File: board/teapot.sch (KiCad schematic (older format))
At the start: 36 parts, among them P1 BATT, P2 SMA, Q1 TEPT4400, U1 TLV61225, U2 microusb-b, U3 RFM69W, U4 STM32L052K8, U5 HTU21D, U6 MS5637, U7 SWD, Y1 32.768k

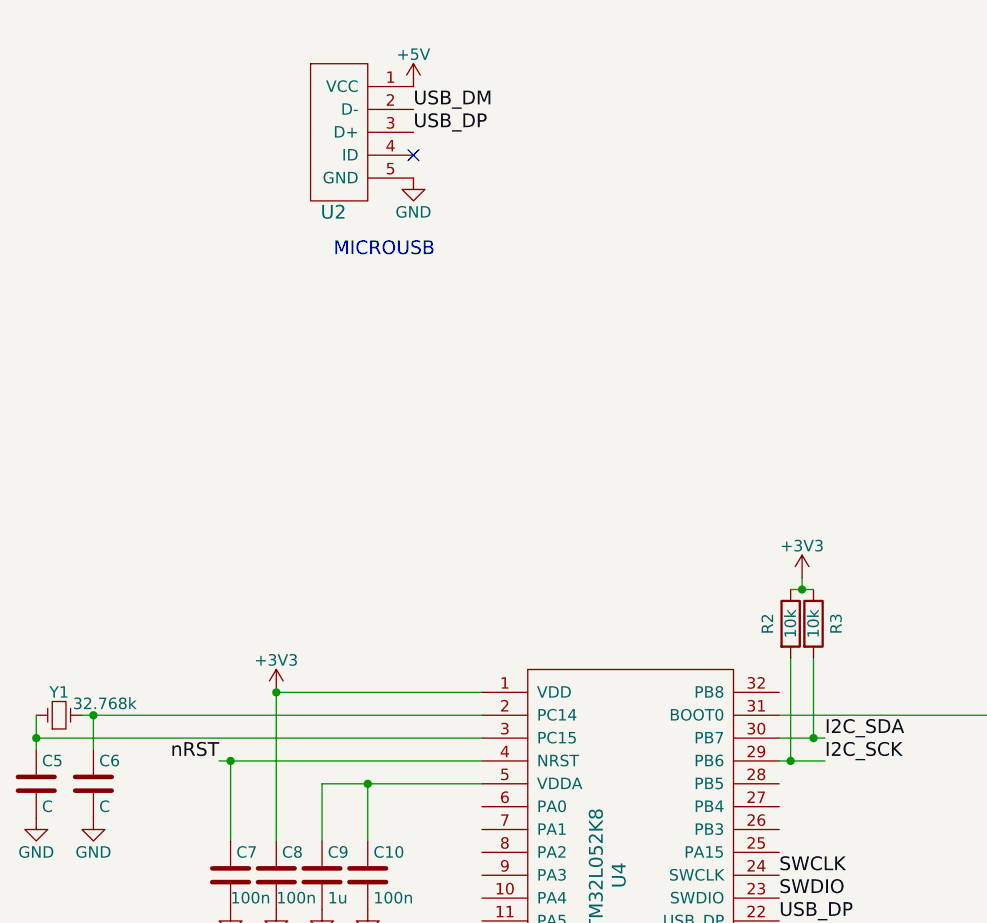
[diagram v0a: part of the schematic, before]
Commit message: Added USB LDO.  Resolves #9
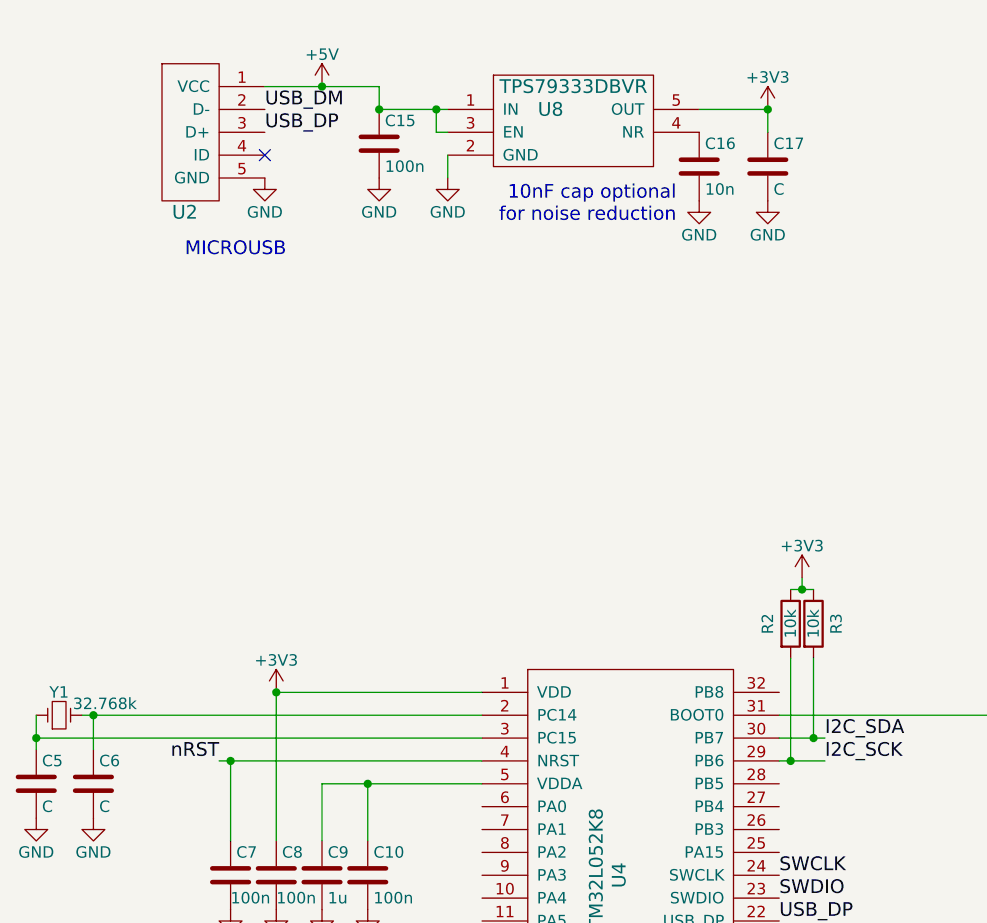
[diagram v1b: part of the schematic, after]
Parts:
- added C15: 100n, symbol C
- added C16: 10n, symbol C
- added C17: C, symbol C
- added U8: TPS79333DBVR, TO_SOT_Packages_SMD:SOT-23-5, symbol TPS79333DBVR
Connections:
- net +3V3: now also C17.1, U8.5 (OUT)
- net +5V: now also C15.1, U8.1 (IN), U8.3 (EN)
- net GND: now also C15.2, C16.2, C17.2, U8.2 (GND)
- new net: C16.1, U8.4 (NR)
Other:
- note added: "10nF cap optional\nfor noise reduction"
- moved on the sheet: U2

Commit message: Added microusb footprint, resolves #6
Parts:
- U2: footprint (none) -> footprints:USB3065
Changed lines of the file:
@@
 F 0 "U2" H 4550 950 60  0000 C CNN
 F 1 "microusb-b" H 4550 850 60  0001 C CNN
-F 2 "" H 4700 1300 60  0000 C CNN
+F 2 "footprints:USB3065" H 4700 1300 60  0001 C CNN
 F 3 "" H 4700 1300 60  0000 C CNN
 	1    4600 1300

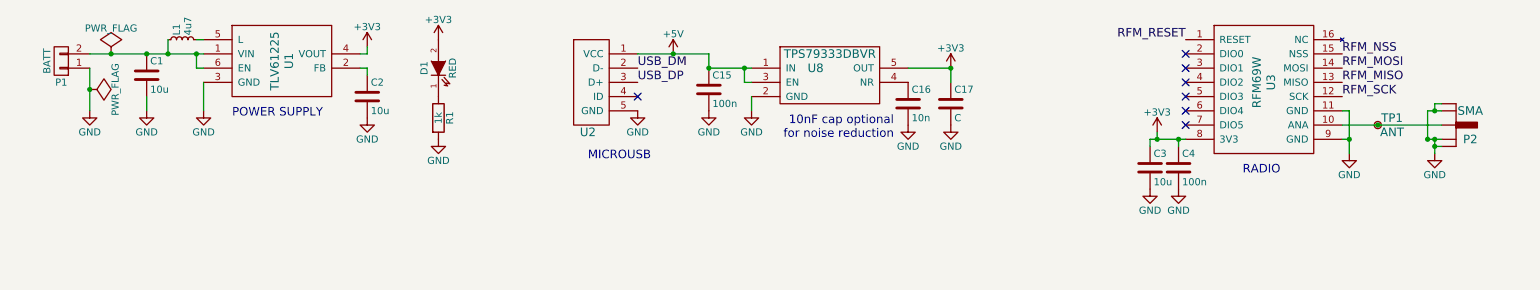
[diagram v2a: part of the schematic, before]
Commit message: Added ESD-protection TVSs. Resolves #7
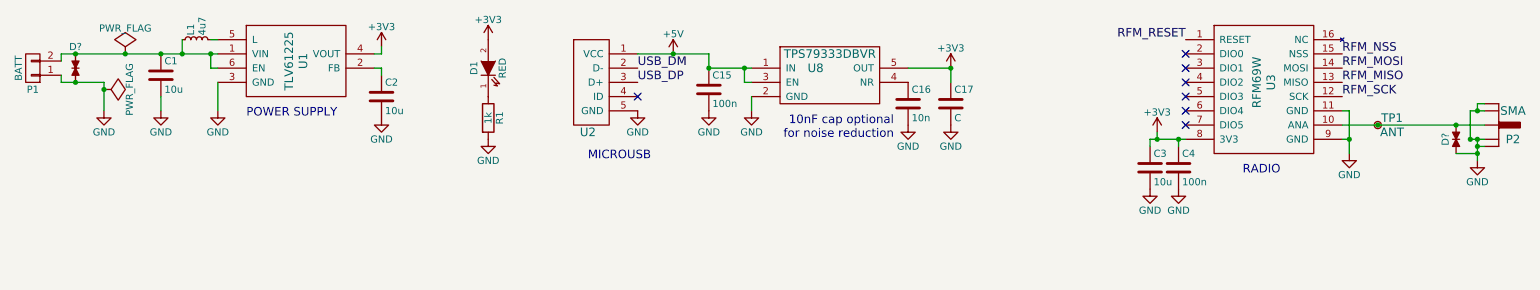
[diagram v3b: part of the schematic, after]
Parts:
- added D? (x2): TVS_small, Resistors_SMD:R_0603, symbol TVS_small
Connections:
- net GND: now also D?.1, D?.2
- net at C1.1, L1.1, P1.2 (P2)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: now also D?.1
- net at P2.1 (RF), TP1.1, U3.10 (ANA): now also D?.2
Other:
- moved on the sheet: C1, C2, D1, L1, P1, P2, R1, U1
